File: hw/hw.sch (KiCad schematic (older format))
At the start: 17 parts, among them U1 74LS299, U2 74LS138, U3 Z80CPU, U4 74LS161, U5 CY7C199, U6 74LS107, X1 CXO_DIP8

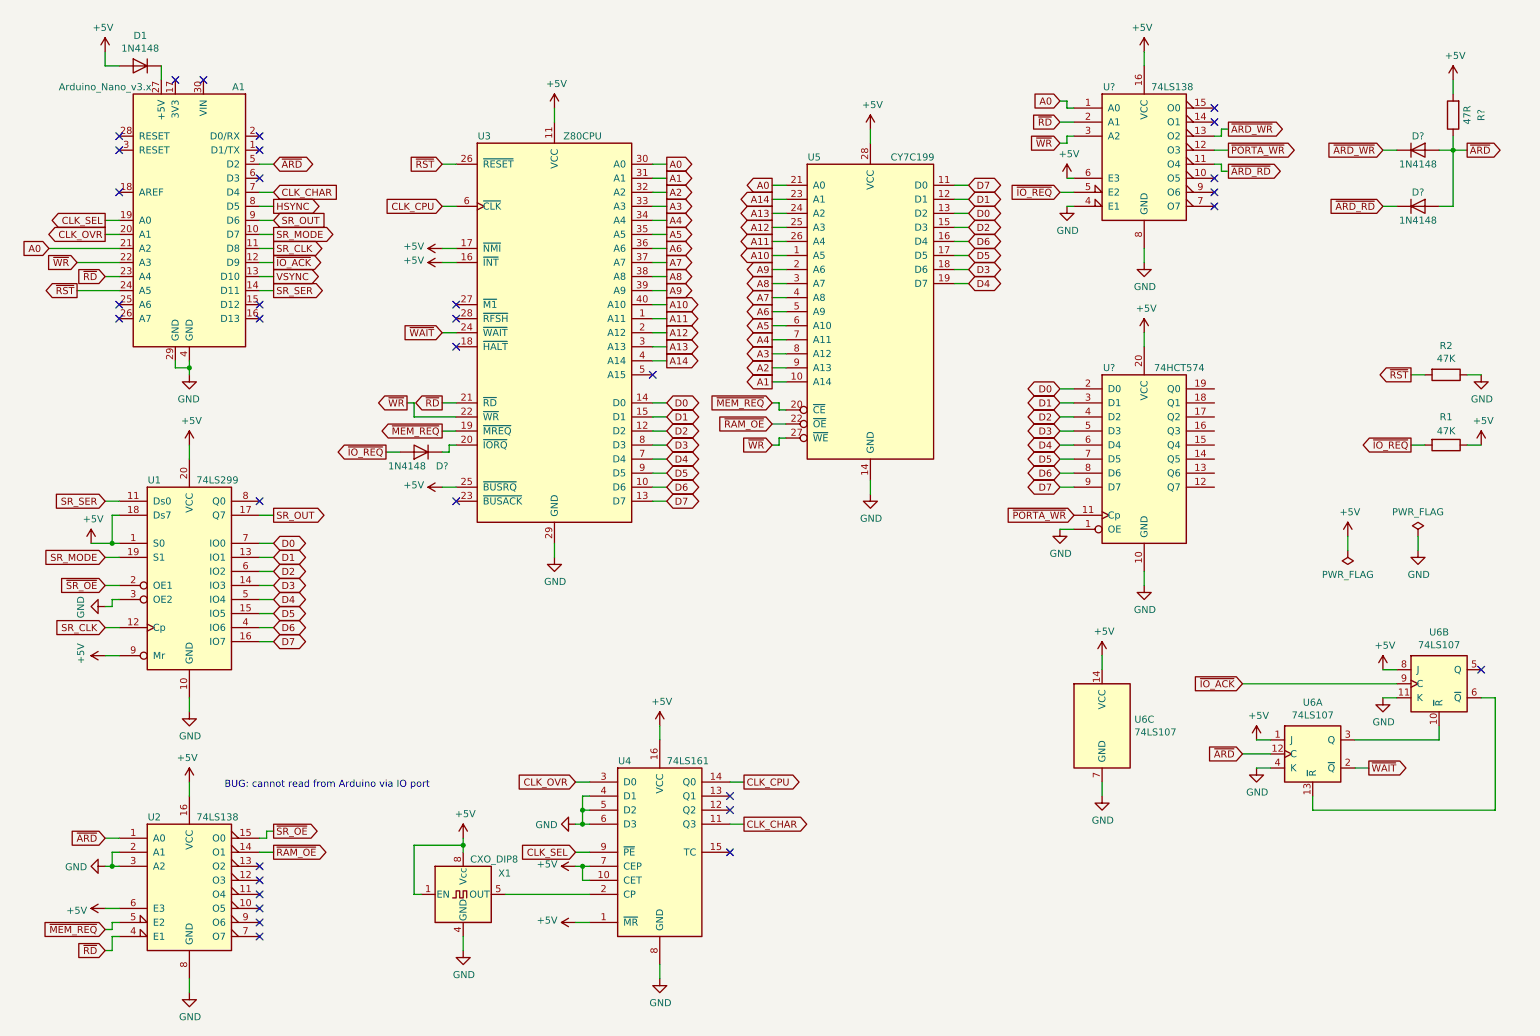
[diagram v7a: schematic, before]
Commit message: add vertical sync interrupt
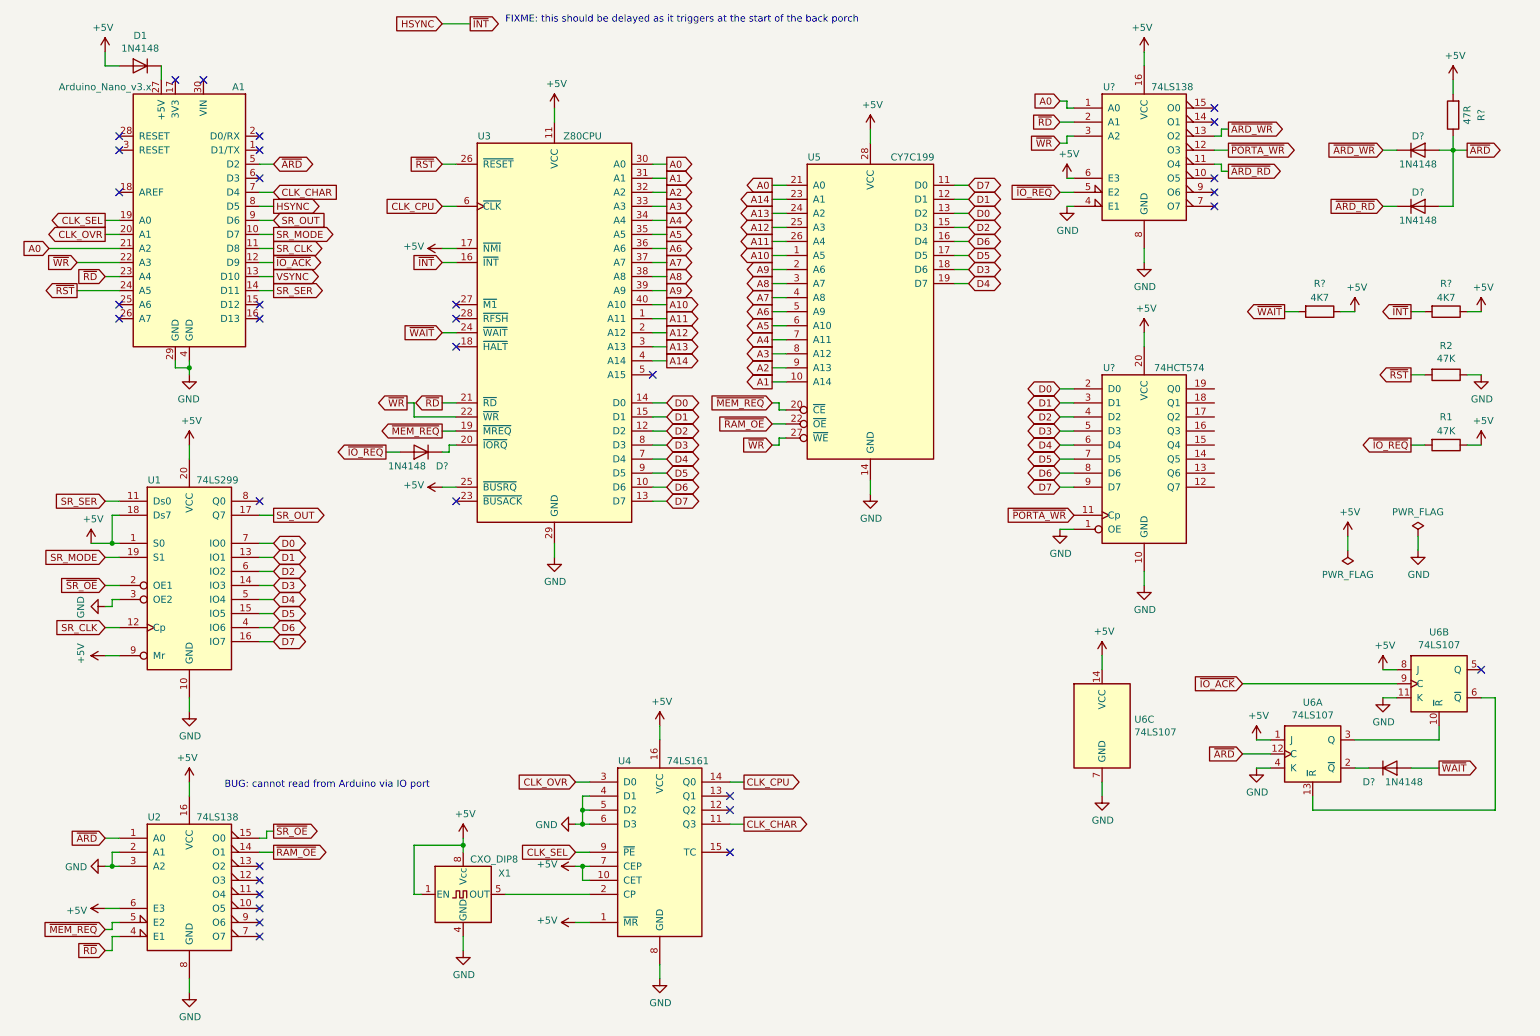
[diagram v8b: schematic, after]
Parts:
- added D?: 1N4148, Diode_THT:D_DO-35_SOD27_P7.62mm_Horizontal, symbol Diode:1N4148
- added R? (x2): 4K7, symbol Device:R
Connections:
- net +5V: now also R?.1, R?.1; no longer U3.16 (~INT~)
- net HSYNC: now also U3.16 (~INT~), R?.2
- net ~WAIT: now also D?.2 (A), R?.2; no longer U6.2 (~Q)
- new net: D?.1 (K), U6.2 (~Q)
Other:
- note added: "FIXME: this should be delayed as it triggers at the start of the back porch"
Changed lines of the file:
@@
-	0    -1   -1   0
-$EndComp
-$Comp
-L power:+5V #PWR0109
-U 1 1 5D29FF98
-P 3500 2300
-F 0 "#PWR0109" H 3500 2150 50  0001 C CNN
-F 1 "+5V" V 3515 2428 50  0000 L CNN
-F 2 "" H 3500 2300 50  0001 C CNN
-F 3 "" H 3500 2300 50  0001 C CNN
-	1    3500 2300
 	0    -1   -1   0
 $EndComp
@@
 Text GLabel 3500 2800 0    50   Input ~ 0
 ~WAIT
-Text GLabel 10100 5900 2    50   Output ~ 0
+Text GLabel 10600 5900 2    50   Output ~ 0
 ~WAIT
 Text GLabel 9200 5300 0    50   Input ~ 0
@@
 Wire Wire Line
 	2300 2400 2200 2400
+Text GLabel 3500 600  0    50   Input ~ 0
+HSYNC
+Text GLabel 3700 600  2    50   Output ~ 0
+~INT
+Wire Wire Line
+	3500 600  3700 600
+Text Notes 3950 600  0    50   ~ 0
+FIXME: this should be delayed as it triggers at the start of the back porch
+Text GLabel 10400 2650 0    50   Output ~ 0
+~INT
+$Comp
+L Device:R R?
+U 1 1 5D712536
+P 10650 2650
+F 0 "R?" V 10450 2650 50  0000 C CNN
+F 1 "4K7" V 10550 2650 50  0000 C CNN
+F 2 "" V 10580 2650 50  0001 C CNN
+F 3 "~" H 10650 2650 50  0001 C CNN
+	1    10650 2650
+	0    1    1    0
+$EndComp
+Wire Wire Line
+	10400 2650 10500 2650
+Wire Wire Line
+	10900 2650 10800 2650
+$Comp
+L power:+5V #PWR?
+U 1 1 5D71253F
+P 10900 2650
+F 0 "#PWR?" H 10900 2500 50  0001 C CNN
+F 1 "+5V" H 10915 2823 50  0000 C CNN
+F 2 "" H 10900 2650 50  0001 C CNN
+F 3 "" H 10900 2650 50  0001 C CNN
+	1    10900 2650
+	1    0    0    -1
+$EndComp
+Text GLabel 3500 2300 0    50   Input ~ 0
+~INT
+Text GLabel 9500 2650 0    50   Output ~ 0
+~WAIT
+$Comp
+L Device:R R?
+U 1 1 5D722C7E
+P 9750 2650
+F 0 "R?" V 9550 2650 50  0000 C CNN
+F 1 "4K7" V 9650 2650 50  0000 C CNN
+F 2 "" V 9680 2650 50  0001 C CNN
+F 3 "~" H 9750 2650 50  0001 C CNN
+	1    9750 2650
+	0    1    1    0
+$EndComp
+Wire Wire Line
+	9500 2650 9600 2650
+Wire Wire Line
+	10000 2650 9900 2650
+$Comp
+L power:+5V #PWR?
+U 1 1 5D722C86
+P 10000 2650
+F 0 "#PWR?" H 10000 2500 50  0001 C CNN
+F 1 "+5V" H 10015 2823 50  0000 C CNN
+F 2 "" H 10000 2650 50  0001 C CNN
+F 3 "" H 10000 2650 50  0001 C CNN
+	1    10000 2650
+	1    0    0    -1
+$EndComp
+$Comp
+L Diode:1N4148 D?
+U 1 1 5D732B67
+P 10250 5900
+F 0 "D?" H 10100 6000 50  0000 C CNN
+F 1 "1N4148" H 10350 6000 50  0000 C CNN
+F 2 "Diode_THT:D_DO-35_SOD27_P7.62mm_Horizontal" H 10250 5725 50  0001 C CNN
+F 3 "http://www.nxp.com/documents/data_sheet/1N4148_1N4448.pdf" H 10250 5900 50  0001 C CNN
+	1    10250 5900
+	1    0    0    1
+$EndComp
+Wire Wire Line
+	10600 5900 10400 5900
 $EndSCHEMATC
